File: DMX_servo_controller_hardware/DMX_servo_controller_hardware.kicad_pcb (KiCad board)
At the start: 4 copper layers, 100 x 100 mm, 64 parts, among them J1 - DMX To_XLR3, J2 - DMX To_XLR3, J3 - PWR Power connector, J4 - DISPLAY Display, J5 - ROT ENC Rotary encoder, J6 Output block 1, J7 Output block 2, J8 Output block 3, J9 Output block 4, Q1 BSS138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

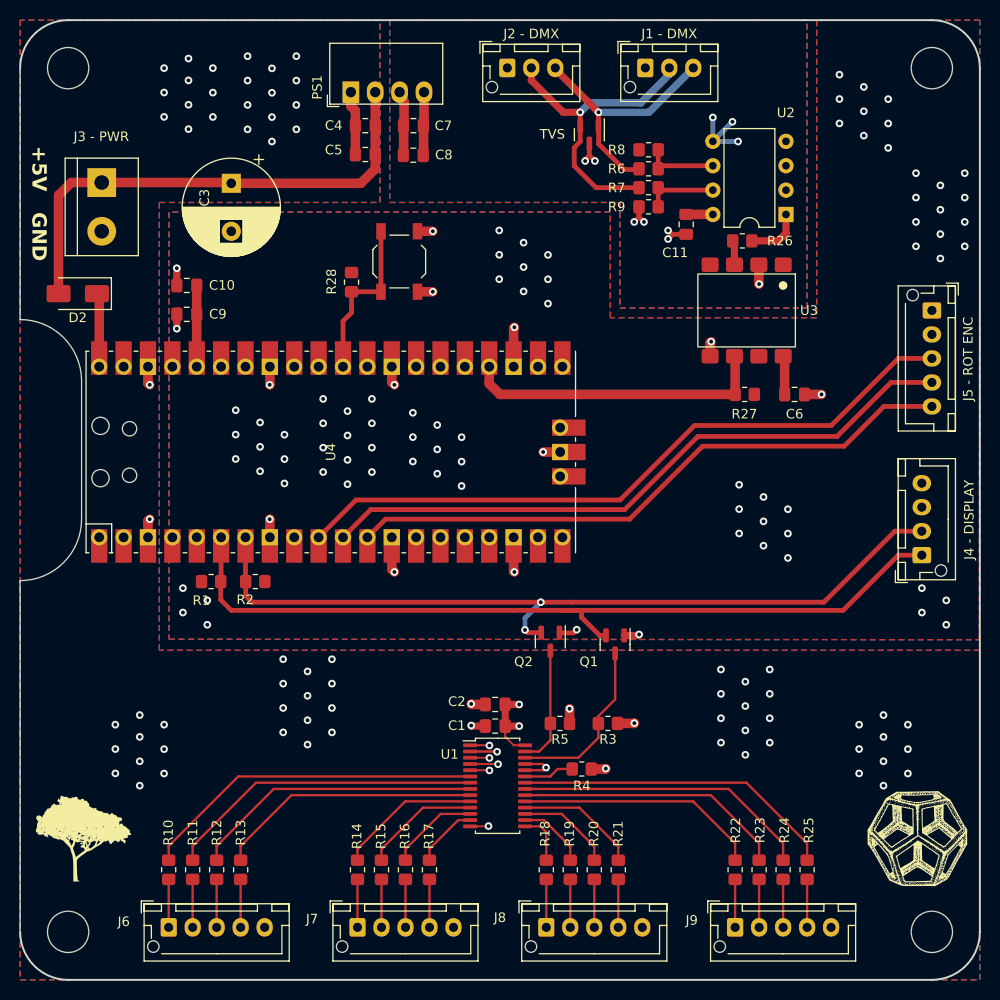
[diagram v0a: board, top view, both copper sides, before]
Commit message: Finalizes PCB
* Changes connector descriptions that didn't match schematics
* Reviews silkscreen
* Minor layout changes
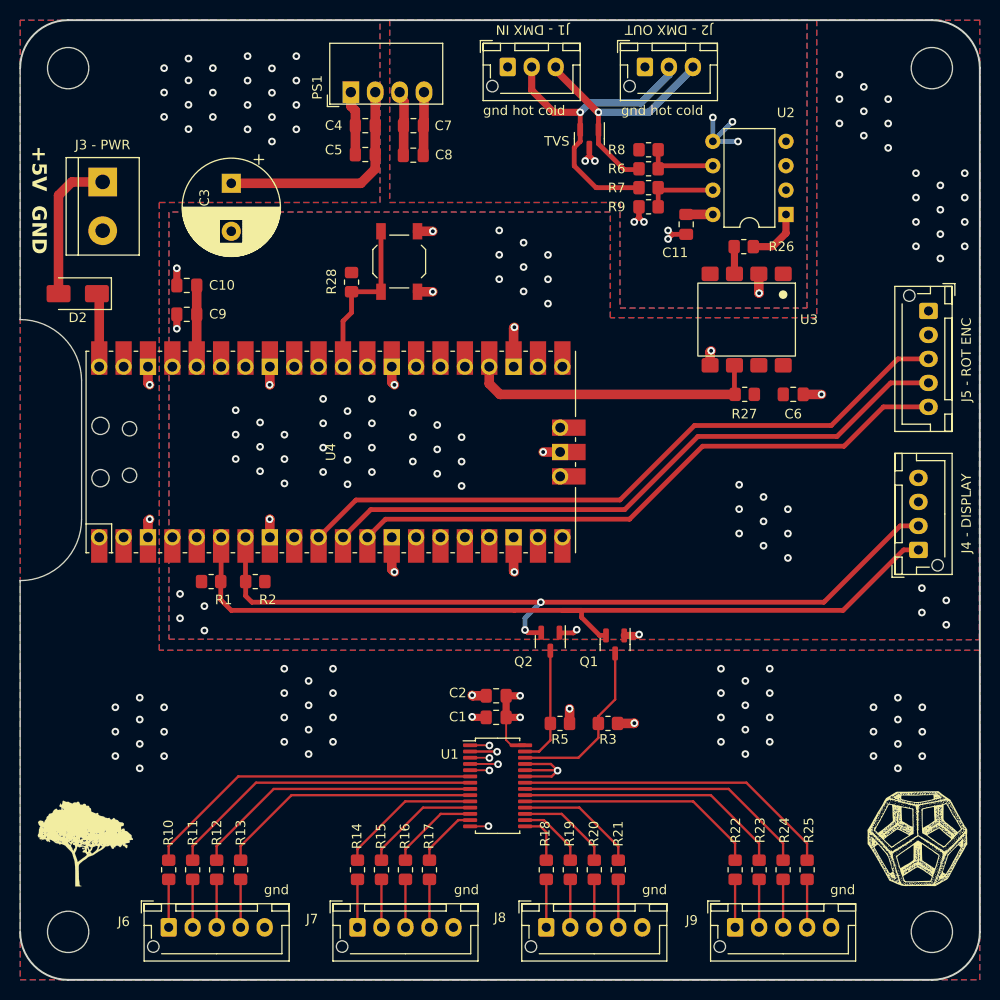
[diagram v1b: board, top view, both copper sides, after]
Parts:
- removed J1 - DMX: To_XLR3, Connector_JST:JST_XH_B3B-XH-AM_1x03_P2.50mm_Vertical
- removed J2 - DMX: To_XLR3, Connector_JST:JST_XH_B3B-XH-AM_1x03_P2.50mm_Vertical
- removed J3 - PWR: Power connector, TerminalBlock:TerminalBlock_bornier-2_P5.08mm
- removed J4 - DISPLAY: Display, Connector_JST:JST_XH_B4B-XH-AM_1x04_P2.50mm_Vertical
- removed J5 - ROT ENC: Rotary encoder, Connector_JST:JST_XH_B5B-XH-AM_1x05_P2.50mm_Vertical
- removed R4: 10kΩ, Resistor_SMD:R_0805_2012Metric_Pad1.20x1.40mm_HandSolder
- removed TVS: SM712_SOT23, Package_TO_SOT_SMD:SOT-23
- added D1: SM712_SOT23, Package_TO_SOT_SMD:SOT-23, F.Cu at (159.3, 72.4)
- added J1: To_XLR3, Connector_JST:JST_XH_B3B-XH-AM_1x03_P2.50mm_Vertical, F.Cu at (150.8, 64.9)
- added J2: To_XLR3, Connector_JST:JST_XH_B3B-XH-AM_1x03_P2.50mm_Vertical, F.Cu at (165.1, 64.9)
- added J3: Power connector, TerminalBlock:TerminalBlock_bornier-2_P5.08mm, F.Cu at (108.6, 76.9)
- added J4: Display, Connector_JST:JST_XH_B4B-XH-AM_1x04_P2.50mm_Vertical, F.Cu at (193.6, 115.2)
- added J5: Rotary encoder, Connector_JST:JST_XH_B5B-XH-AM_1x05_P2.50mm_Vertical, F.Cu at (194.7, 90.3)
- moved U3 0.95 mm to (175.7, 91.2)
- moved C1 0.91 mm to (149.6, 132.7)
- moved C2 0.91 mm to (149.6, 130.4)
- moved R26 0.62 mm to (175.4, 83.6)
- moved Ref** 0.55 mm to (106.8, 145.8)
- moved C6 0.15 mm to (180.6, 99.0)
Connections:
- U1 pad 23: Net-(U1-~{OE}) -> GND
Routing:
- net +5V: track 64.5 -> 52.2 mm
- net Net-(U1-~{OE}): track 5.23 -> 0.00 mm
- net GND: track 62.4 -> 66.9 mm, vias 85 -> 84
- net +3.3V: track 16.1 -> 12.0 mm
- net DMX_signal: track 31.9 -> 30.9 mm
- net DMX_positive/hot: track 32.9 -> 33.6 mm
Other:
- board text added: "J1 - DMX IN"
- board text added: "J2 - DMX OUT"
- board text added: "J3 - PWR"
- board text added: "J4 - DISPLAY"
- board text added: "J5 - ROT ENC"
- board text added: "TVS"
- board text added: "gnd"
- board text added: "gnd hot cold"
